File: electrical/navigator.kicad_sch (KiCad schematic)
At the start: 12 parts

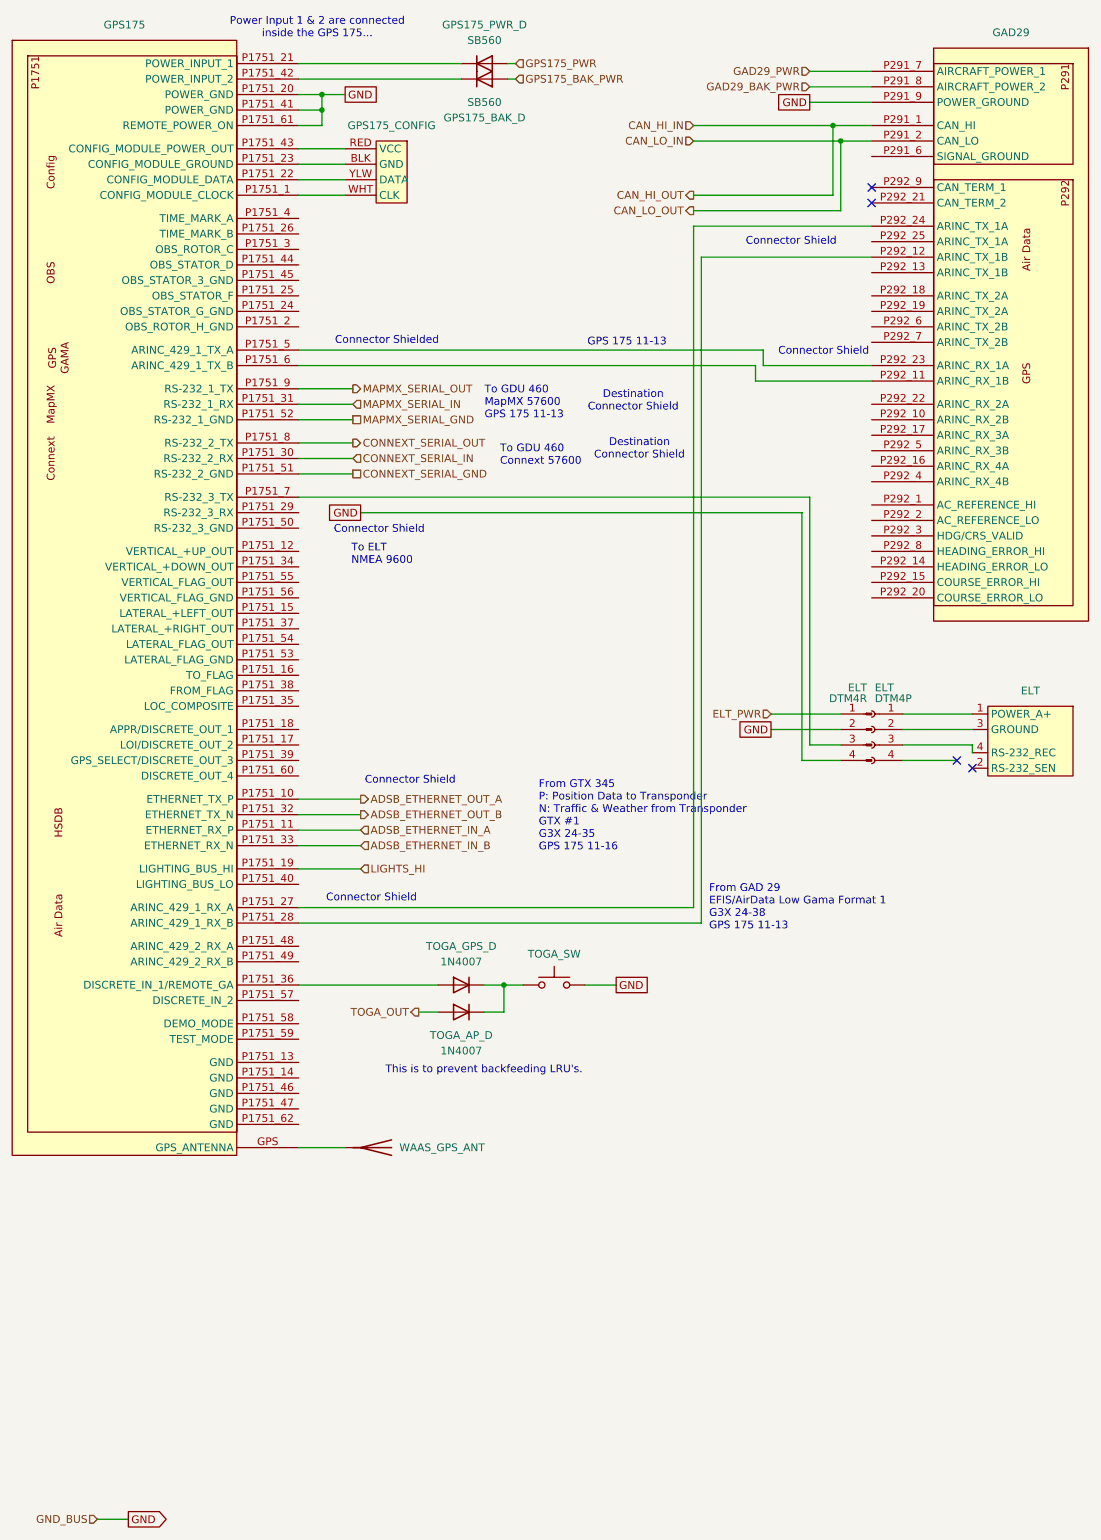
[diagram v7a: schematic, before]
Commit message: Added shielding and wire colors and corrections.
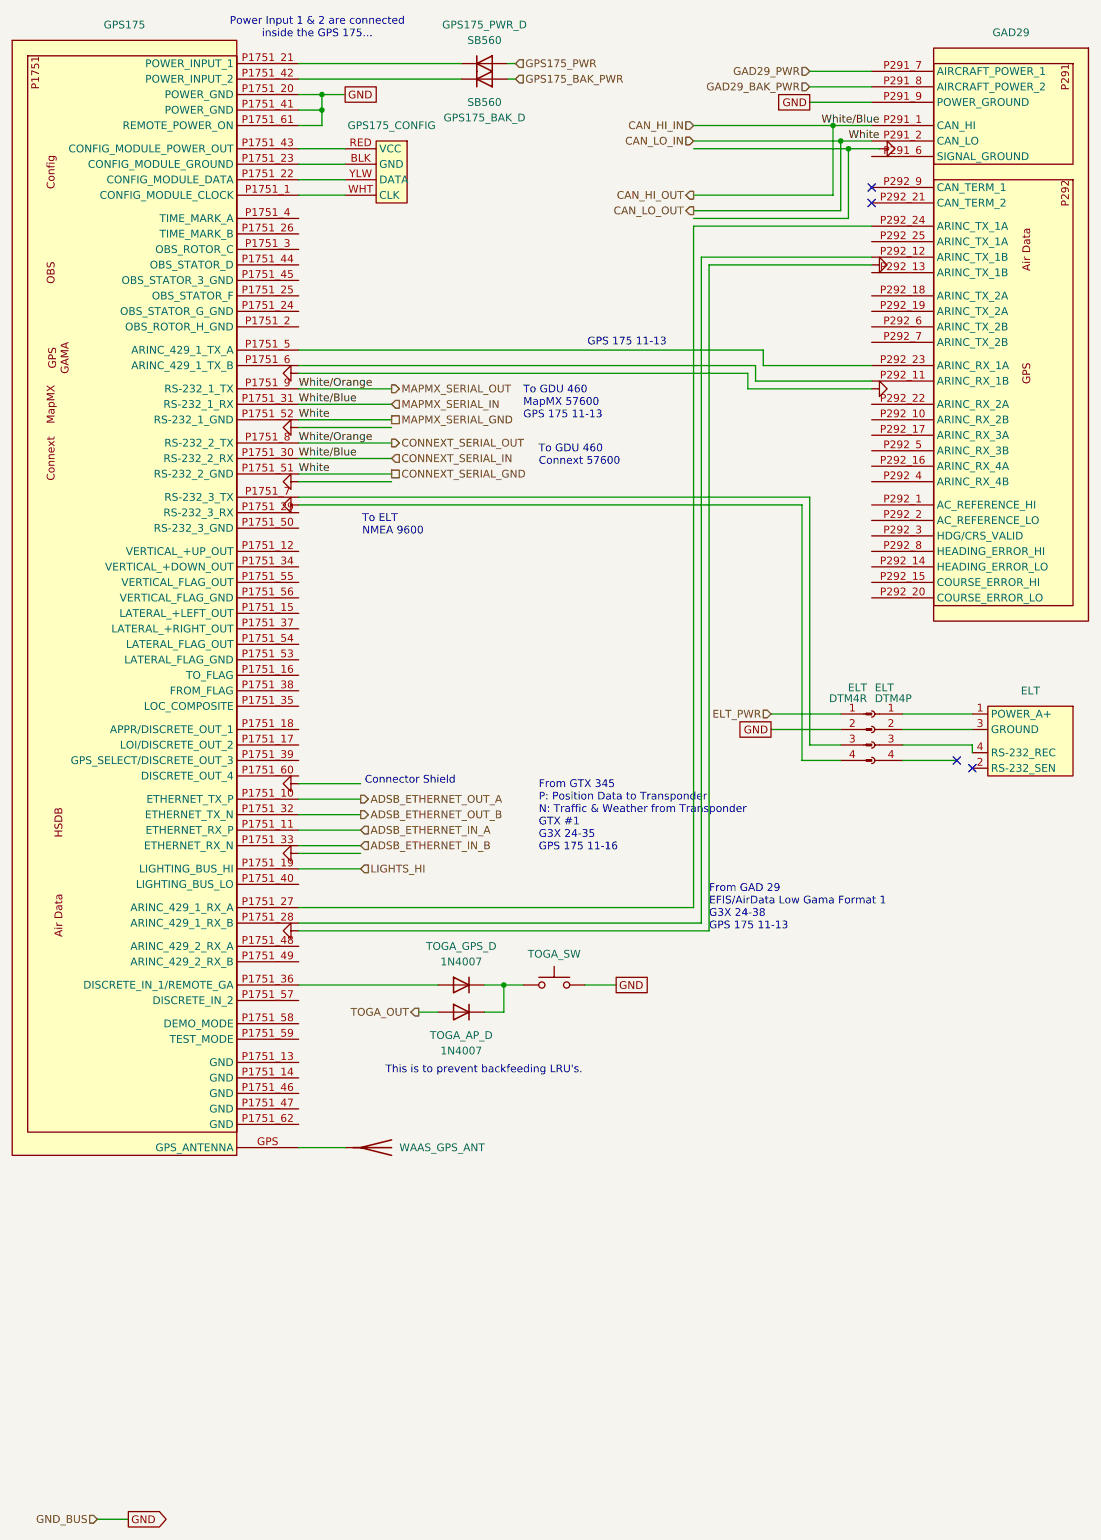
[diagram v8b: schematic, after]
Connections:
- net MAPMX_SERIAL_GND is gone; now on net CONNEXT_SERIAL_GND: GPS175.P1751_52 (RS-232_1_GND)
- net MAPMX_SERIAL_IN is gone; now on net CONNEXT_SERIAL_IN: GPS175.P1751_31 (RS-232_1_RX)
- net MAPMX_SERIAL_OUT is gone; now on net CONNEXT_SERIAL_OUT: GPS175.P1751_9 (RS-232_1_TX)
- net GND: no longer ELT.4 (Pin_4)
- new net GNDS: ELT.4 (Pin_4)
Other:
- note removed: "Connector Shielded"
- note removed: "Destination Connector Shield"
